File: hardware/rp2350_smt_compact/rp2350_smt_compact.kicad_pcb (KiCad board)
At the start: 2 copper layers, 50 x 35 mm, 26 parts, among them J1 RP2350_Zero_Header_23p, J2 USB_A_Neltron_5075AR-04-WH, J3 RP2350_Zero_Header_23p, SW1 SW_SPDT_NKK_115643_Slide, SW2 SW_SPDT_NKK_115643_Slide, SW3 SW_SPDT_NKK_115643_Slide, SW4 SW_SPDT_NKK_115643_Slide, SW5 SW_SPDT_NKK_115643_Slide, SW6 SW_TACT_Akizuki_DTS63, U1 TPS2051BDBVR, U2 USBLC6-2SC6, U3 USBLC6-2SC6

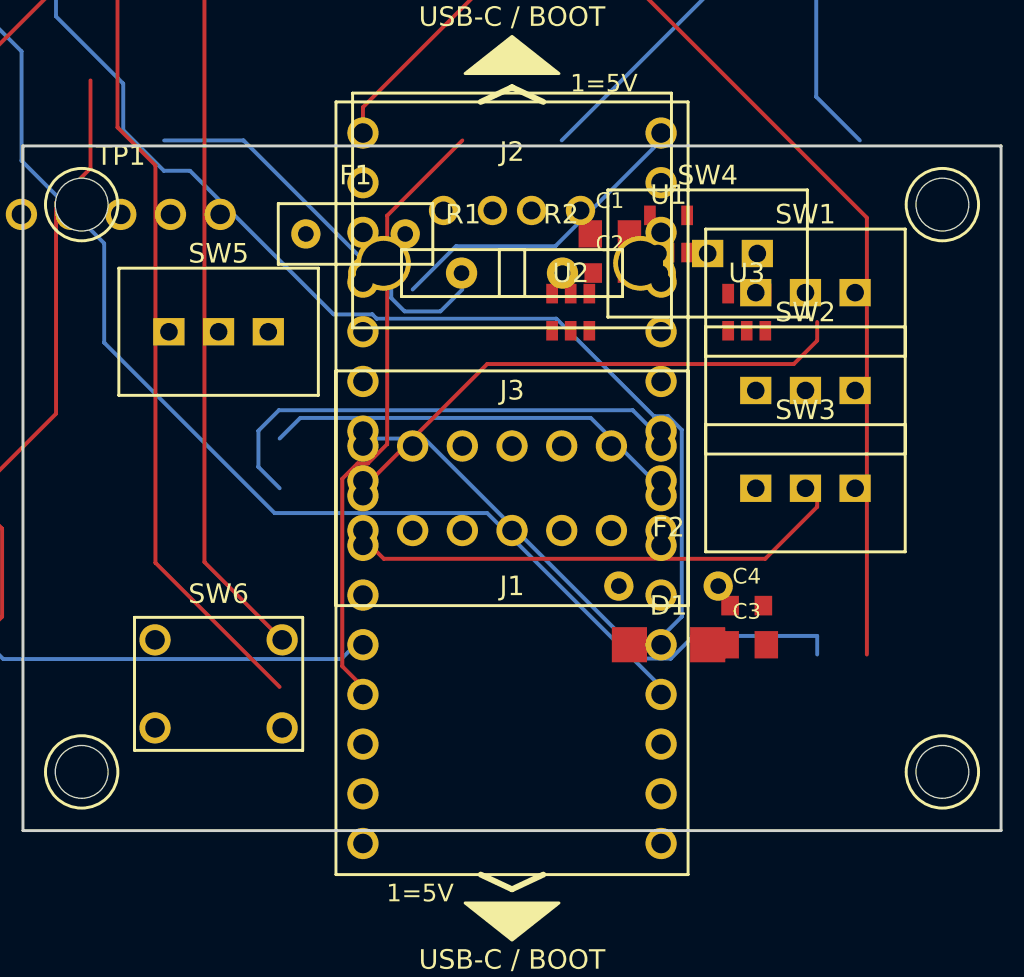
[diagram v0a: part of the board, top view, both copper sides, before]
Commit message: review: fix SMT compact carrier inconsistencies
- kicad_pcb: R1/R2 を THT axial (through_hole, P10.16mm, drill0.8) から SMD 0603 (0.9x1.0mm, smd, gap0.8) に修正。pretty の R_0603 と一致、JLC Basic 手ハンダ可能パッケージに準拠。BOM 誤記 C25804(10k) を正しい 22Ω 0603 C22902 に整合
- kicad_pcb: J1/J3 を through_hole 円パッドから RP2350_Zero_SMT_23p_Castellated の正規 smd 矩形+NPTH 半穴定義 (attr smd) に置換。pretty と一致し Castellated Holes 指定を正しく表現。J3 5V を J3_VBUS_5V ネットに接続
- kicad_pcb: SW1-SW5 を THT 3pin (through_hole) から SMスライド SS-12D00G3 SMD 5pad ガルウィング (attr smd, 1.2x1.5mm, anchor 4/5 追加) に置換、SW6 を THT 4pin から PTS645 SMD 6x6 (4pad gull-wing) に置換。pretty と整合
- kicad_pcb: U1 TPS2051B SOT23-5 の未接続パッドにネット割当 (1=GND,2=VBUS_USB_A,3=GND(EN pull-down),4=VBUS_USB_A_SW)。D1/F2/C1-C4 の VBUS/GND ネットも補完
- kicad_sch: U1 EN と GND ピンの浮きを解消 (GND ラベルへ配線)、J3 5V→F2→D1 系と C3/C4 のデカップリングのラベル配線を追加 (いずれもホットプラグ突入対策)。U1 IN=VBUS_USB_A(F1後), OUT=VBUS_USB_A_SW(J2) の既定経路は変更なし
- pretty: 未使用 THT フットプリント 4種 (R_Axial_THT_P10.16mm, SW_SPDT_NKK_115643_Slide, SW_TACT_Akizuki_DTS63, RP2350_Zero_Header_23p) を削除。SMT試作の冗長性解消。残り13種は全て SMD/手ハンダ可能のみ
- bom.csv: R1/R2 の LCSC 誤記修正と備考追記

Edge.Cuts 50x35mm, 2チップ縦並び, 既存 carrier 非破壊, fp-lib-table 整合, USB4105 将来 QFN 言及は維持
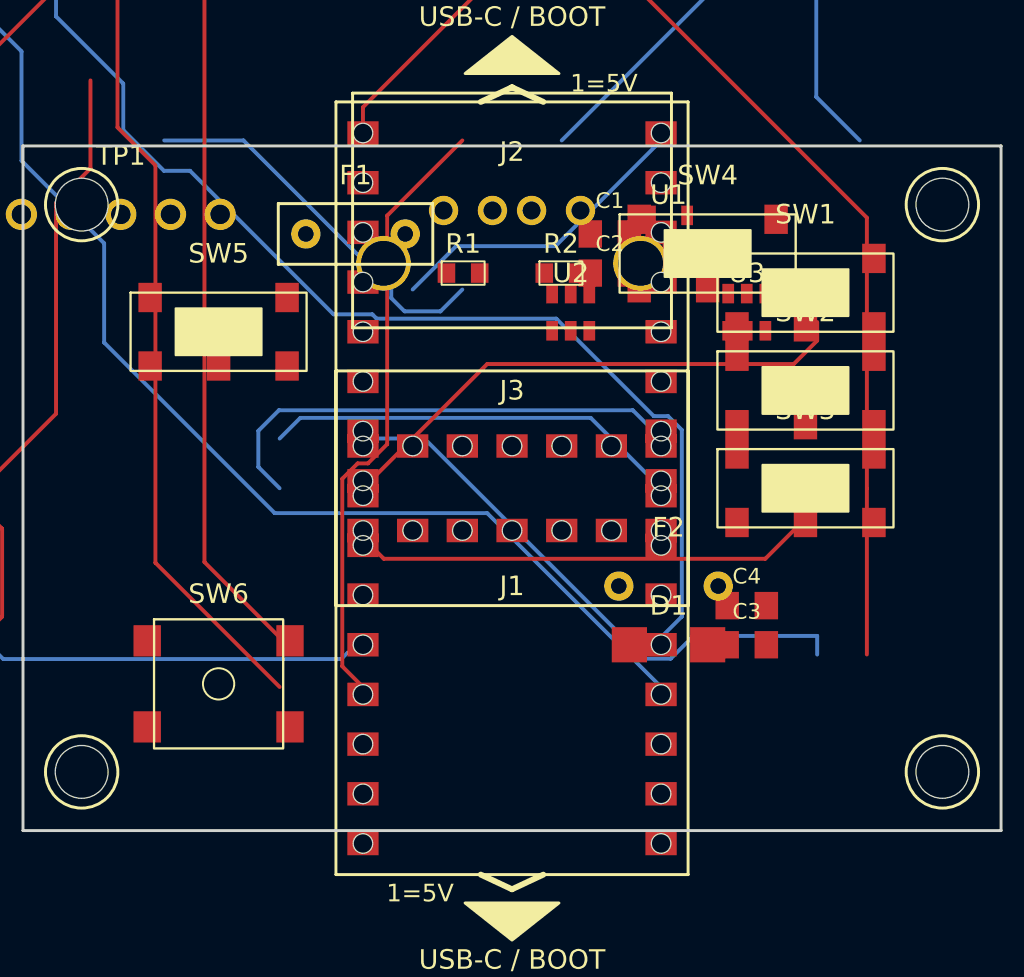
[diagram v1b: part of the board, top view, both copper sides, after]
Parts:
- R1, R2: value R_Axial_THT_P10.16mm -> 22R 0603
- SW1, SW2, SW3, SW4, SW5: value SW_SPDT_NKK_115643_Slide -> SS-12D00G3 SMD SPDT
- SW6: value SW_TACT_Akizuki_DTS63 -> PTS645 SMD 6x6 Tact
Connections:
- C1 pad 1: (no net) -> VBUS_5V
- C1 pad 2: (no net) -> GND
- C2 pad 1: (no net) -> VBUS_5V
- C2 pad 2: (no net) -> GND
- C3 pad 1: (no net) -> J3_VBUS_5V
- C3 pad 2: (no net) -> GND
- C4 pad 1: (no net) -> J3_VBUS_5V
- C4 pad 2: (no net) -> GND
- D1 pad 1: (no net) -> J3_VBUS_5V
- F2 pad 1: (no net) -> J3_VBUS_5V
- F2 pad 2: (no net) -> J3_VBUS_5V
- U1 pad 1: (no net) -> GND
- U1 pad 2: (no net) -> VBUS_USB_A
- U1 pad 3: (no net) -> GND
- U1 pad 4: (no net) -> VBUS_USB_A_SW

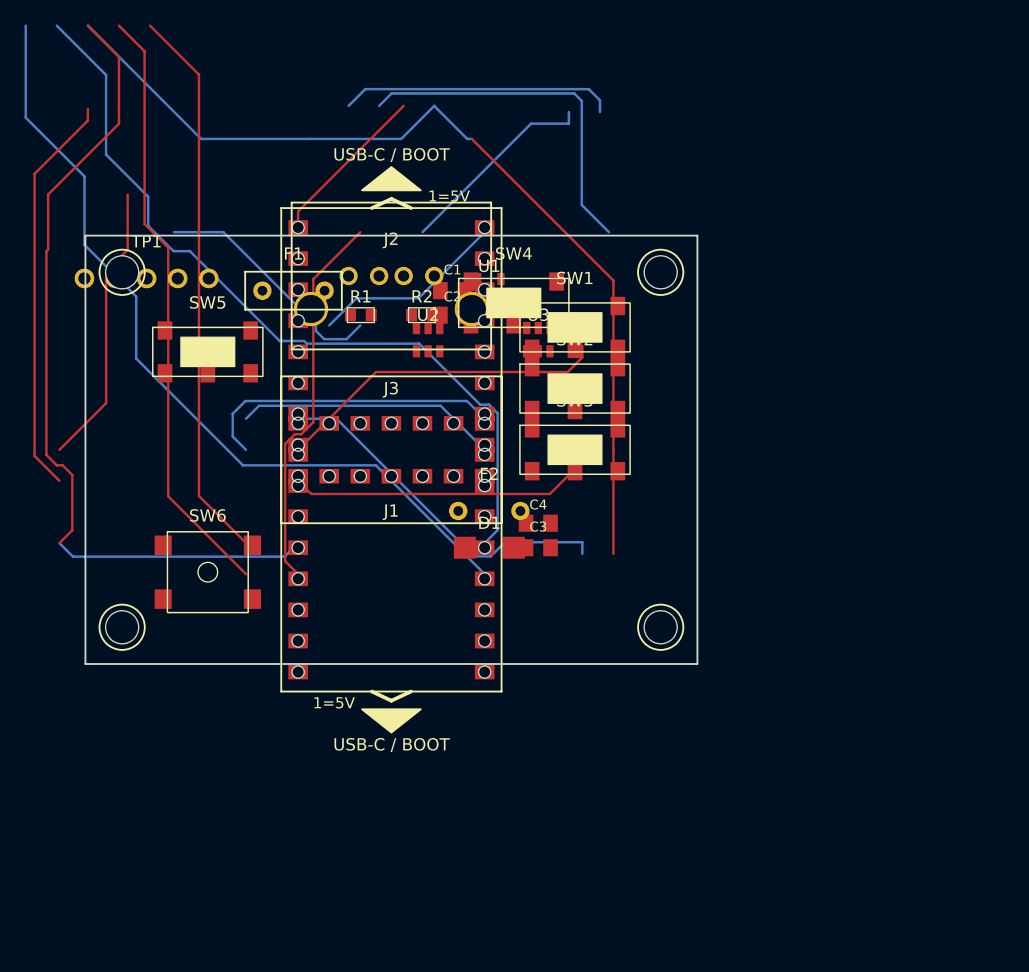
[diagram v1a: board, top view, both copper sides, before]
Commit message: pcb: 配置確認用に配線を除去、Footprint配置のみを整理
- segment/via/zone を全削除し Edge.Cuts (50x35mm) のみに
- J1(0,8)/J3(0,-8 180°)縦並び・J2(0,-14.2)維持
- VBUS系をJ2近傍で横並び等間隔に: C1(-7,-10)/C2(-3,-10)/C3(3,-10)/C4(7,-10)、U1(-4,-12.5)/D1(4,-12.5)、F1(-9,3)/F2(-9,-3)
- データ系を中央に: R1(-2.5,-7)/R2(2.5,-7)、U2(-5,2)/U3(5,2)
- SW類を側面整列: 右側 SW1-4 (16,9/4/-1/-6)、左側 SW5(-16,-4)/SW6(-16,9)、TP1(-18,-14)
- 取付穴H1-H4四隅は維持、3Dビューワで重なり・はみ出し無しを確認するための配置確認用コミット
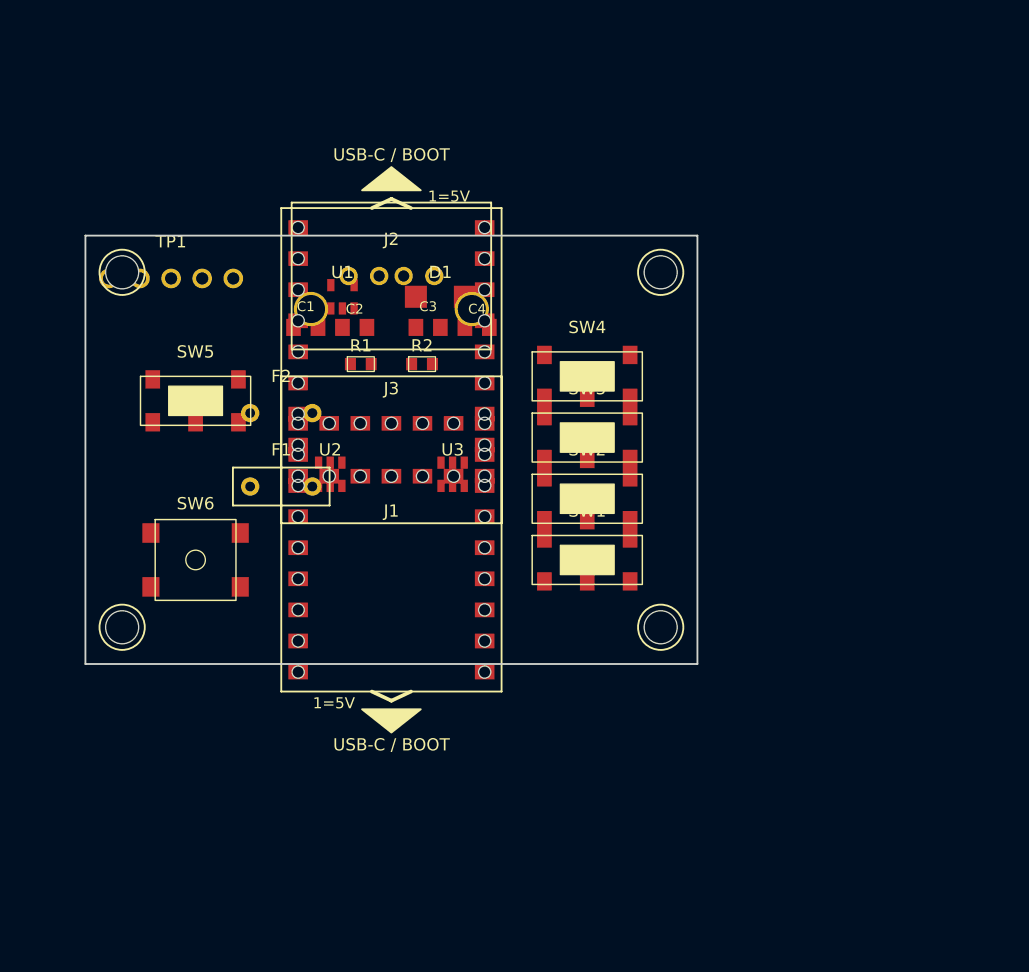
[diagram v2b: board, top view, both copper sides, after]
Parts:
- moved D1 20.9 mm to (4.00, -12.5)
- moved C3 20.1 mm to (3.00, -10.0)
- moved SW1 19.0 mm to (16.0, 9.00)
- moved F2 18.8 mm to (-9.00, -3.00)
- moved C4 16.8 mm to (7.00, -10.0)
- moved F1 16.0 mm to (-9.00, 3.00)
- moved U2 13.6 mm to (-5.00, 2.00)
- moved U3 13.0 mm to (5.00, 2.00)
- moved C1 12.4 mm to (-7.00, -10.0)
- moved U1 12.0 mm to (-4.00, -12.5)
- moved SW2 9.06 mm to (16.0, 4.00)
- moved SW4 8.49 mm to (16.0, -6.00)
- moved C2 8.06 mm to (-3.00, -10.0)
- moved SW5 4.12 mm to (-16.0, -4.00)
- moved R1 4.00 mm to (-2.50, -7.00)
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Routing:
- net GND: track 143.9 -> 0.00 mm
- net GP0_UART0_TX: track 66.7 -> 0.00 mm
- net GP1_UART0_RX: track 65.4 -> 0.00 mm
- net J3_GP0_UART0_TX: track 49.1 -> 0.00 mm
- net J3_GP1_UART0_RX: track 45.5 -> 0.00 mm
- net GP29_SW5_SUSTAIN: track 33.0 -> 0.00 mm
- net VBUS_5V: track 31.2 -> 0.00 mm
- net GP27_SW3_SPARE: track 29.3 -> 0.00 mm
- net USB_A_DM: track 28.9 -> 0.00 mm
- net GP28_SW1_GAME_MODE: track 27.3 -> 0.00 mm
- net GP29_SW2_LYRE_MODE: track 25.7 -> 0.00 mm
- net UART_MIRROR_RETURN: track 25.0 -> 0.00 mm
- net GP28_SW6_RESET: track 23.2 -> 0.00 mm
- net VBUS_USB_A_SW: track 22.4 -> 0.00 mm
- net UART_MIRROR: track 21.4 -> 0.00 mm
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
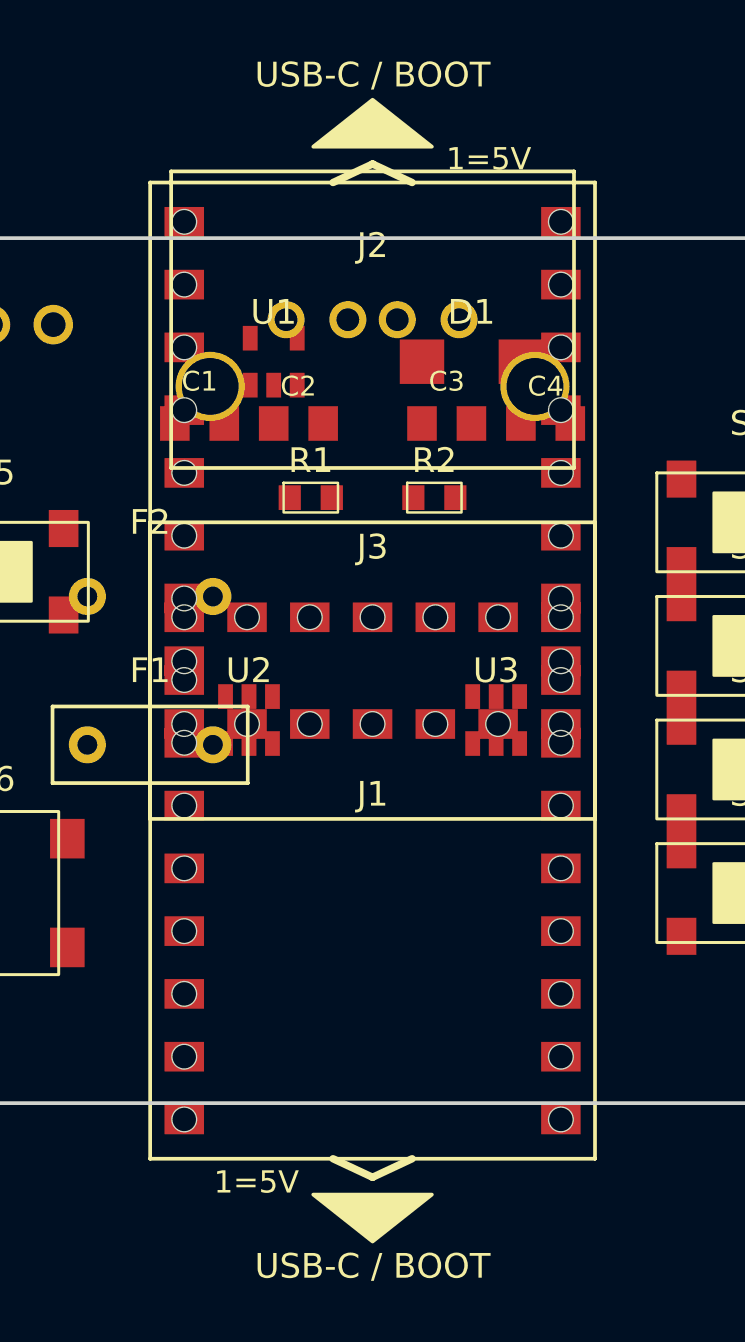
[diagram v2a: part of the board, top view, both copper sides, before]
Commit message: pcb: ピンソケットTHT除去確認 & Zeroはみ出し修正
- J1/J3 は前回レビュー(b5e09fe)で FHU/PH系 THTピンソケットから RP2350_Zero_SMT_23p_Castellated (SMD+NPTH半穴) へ完全置換済みを確認: pcb内の thru_hole パッドは F1/F2(PTC)2+2, J2(USB-A)6, TP1 5, H1-4のみ、np_thru_hole 46は半穴のみ。FHU-1x42SG/PH-1x40SG 等の文字列は pcb/sch/pretty いずれにも残存なし。pretty の RP2350_Zero_Header_23p 等 THT 4種は削除済み
- kicad_sch の J1/J3 は Conn_01x20→Castellatedフットプリント指定のままでピンソケットシンボル残存なしを確認
- はみ出し: Zero 18x23mm を Edge.Cuts 50x35mm 内に収めるため J1(0,8)→(0,6)、J3(0,-8 180°)→(0,-6 180°)へ 2mm内側に移動。J1上端 6+11.5=17.5、J3下端 -6-11.5=-17.5で Edge.Cuts にジャスト収まり(シルク余分0.25mmは許容)、3Dビューワで長いピンの突き出し無しを確認
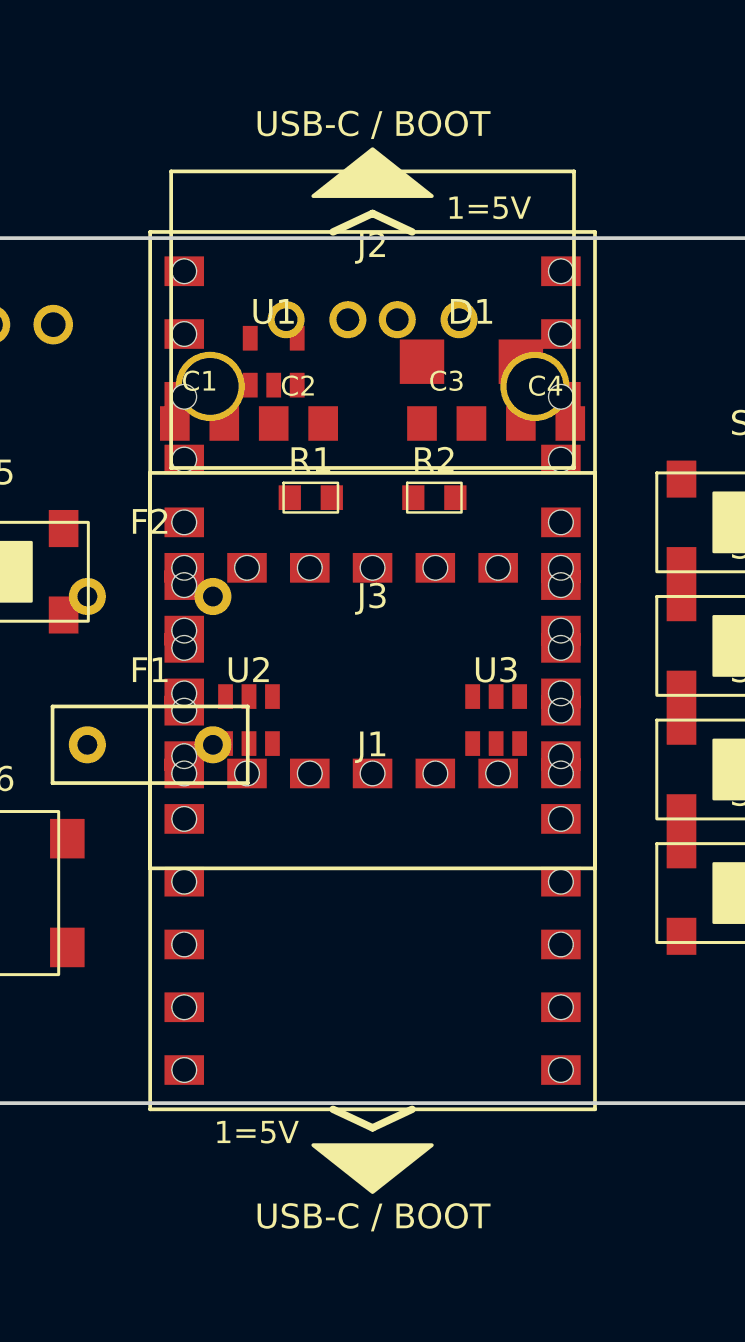
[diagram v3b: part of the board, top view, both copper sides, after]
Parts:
- J1, J3: value RP2350_Zero_Header_23p -> RP2350_Zero_SMT_Castellated
- moved J1 2.00 mm to (0.00, 6.00)
- moved J3 2.00 mm to (0.00, -6.00)
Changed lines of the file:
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@@
 		(footprint "rp2350_smt_compact:RP2350_Zero_SMT_23p_Castellated"
 		(layer "F.Cu")
-		(at 0 8)
+		(at 0 6)
 		(property "Reference" "J1"
 			(at 0 -3 0)
@@
 			)
 		)
-		(property "Value" "RP2350_Zero_Header_23p"
+		(property "Value" "RP2350_Zero_SMT_Castellated"
 			(at 0 3 0)
 			(unlocked yes)
@@
 		(footprint "rp2350_smt_compact:RP2350_Zero_SMT_23p_Castellated"
 		(layer "F.Cu")
-		(at 0 -8 180)
+		(at 0 -6 180)
 		(property "Reference" "J3"
 			(at 0 -3 0)
@@
 			)
 		)
-		(property "Value" "RP2350_Zero_Header_23p"
+		(property "Value" "RP2350_Zero_SMT_Castellated"
 			(at 0 3 0)
 			(unlocked yes)

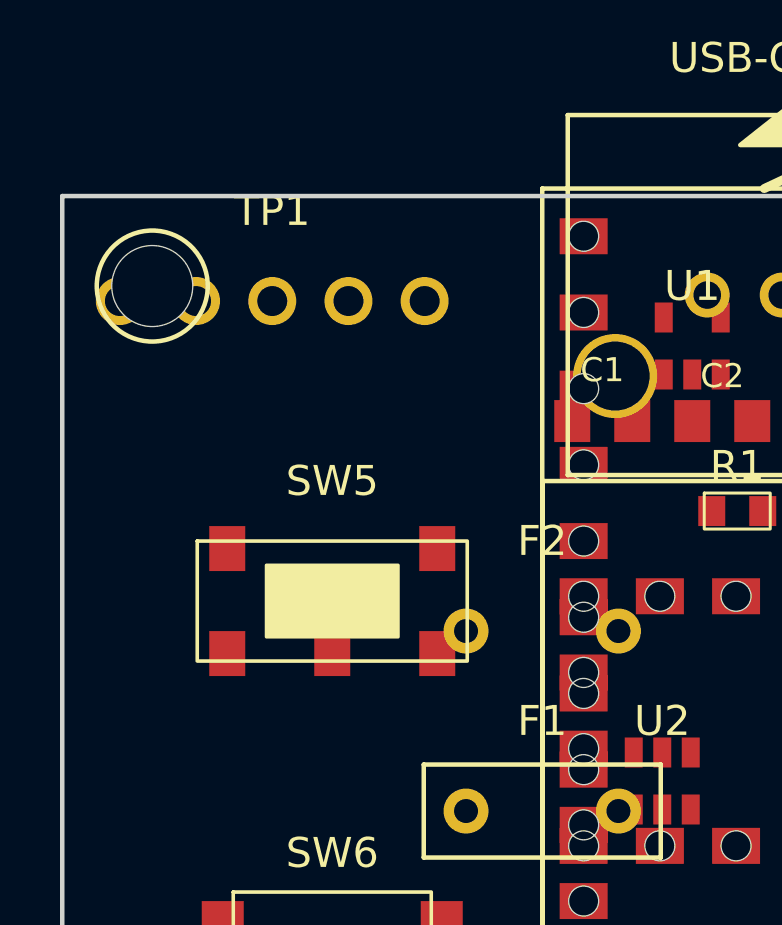
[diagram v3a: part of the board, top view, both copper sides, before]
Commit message: pcb: ネジ穴とUART重なり解消
- H1-H4(-22/22,±14.5)とTP1(-18,-14)が近接しパッド-穴クリアランス0.5mm未満だったため TP1を中央寄り(-14,0)へ移動。H1-H4は四隅のまま維持
- 移動後 H3(-22,-14.5)-TP1(-14,0)中心間16.56mm、パッドエッジ間>2.3mmで0.5mmクリアランスを確保。J1/J3 GP0/1(0,±6)やC/R(-7/-3/3/7,-10)、U2/U3との距離も>4mmで重なり0。3Dビューワでネジ穴とUARTパッドの干渉なしを確認
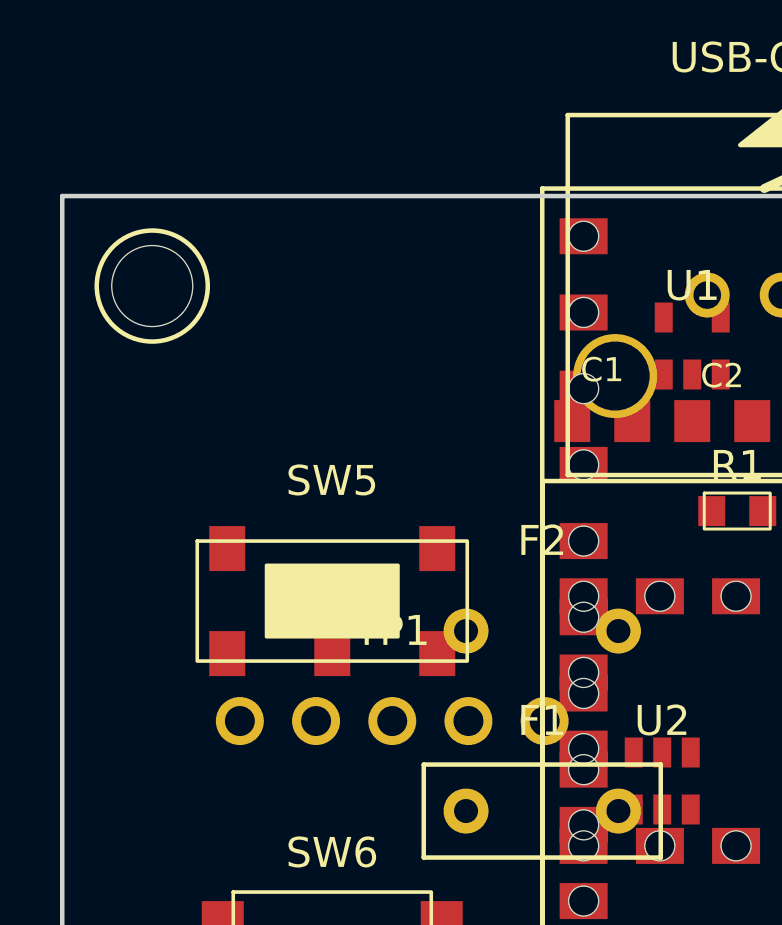
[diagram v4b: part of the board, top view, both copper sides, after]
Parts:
- moved TP1 14.6 mm to (-14.0, 0.00)
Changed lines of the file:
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@@
 	(footprint "rp2350_smt_compact:TestPoint_UART0_1x5_P2.54mm"
 		(layer "F.Cu")
-		(at -18 -14)
+		(at -14 0)
 		(property "Reference" "TP1"
 			(at 0 -3 0)
